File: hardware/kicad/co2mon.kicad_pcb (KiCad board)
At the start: 2 copper layers, 58 x 41 mm, 57 parts, among them J1 SCD30_Conn, J10 TFT_Conn, J11 OLED_Conn, J2 MH_Conn, J3 Z19B_Conn2, J4 T67xx_Conn, J5 Z14A_Conn, J6 Z19B_Conn1, J7 USB_B_Micro, J8 SD_Conn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

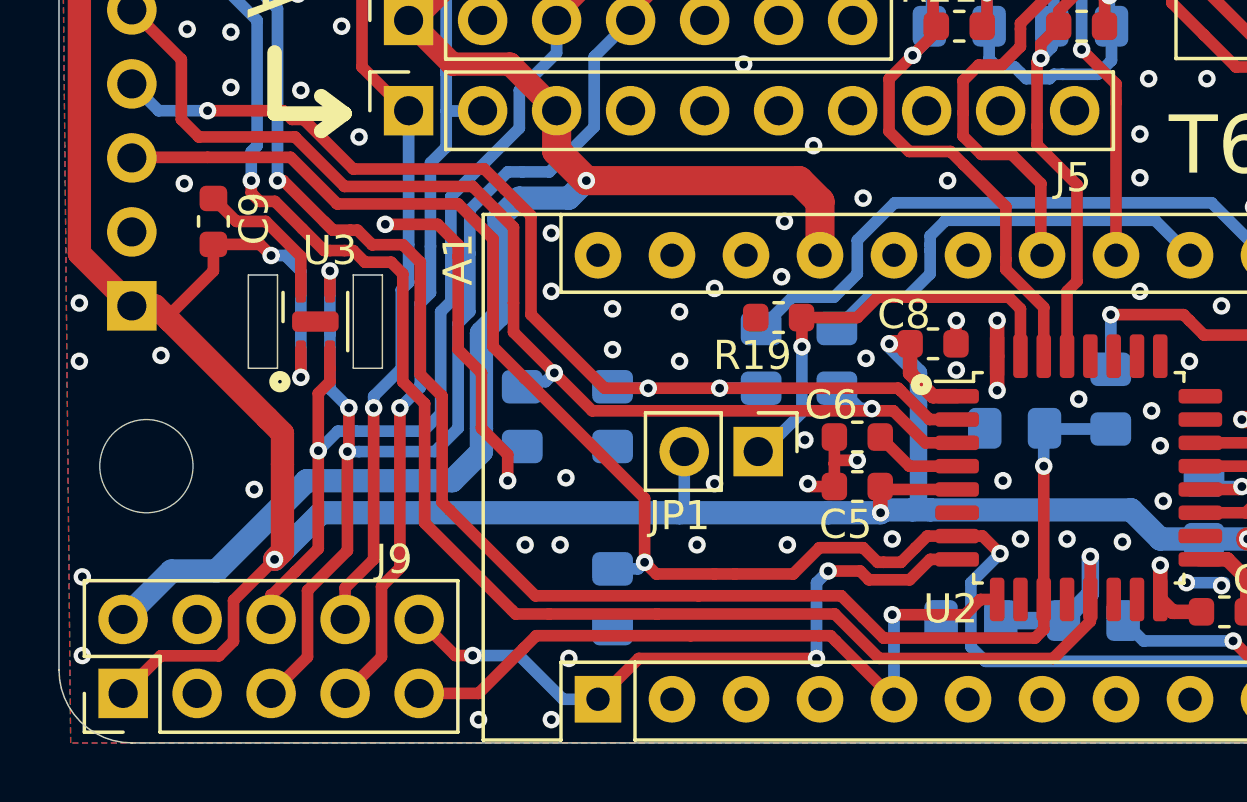
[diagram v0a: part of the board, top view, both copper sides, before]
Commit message: remove temp/humidity sensor
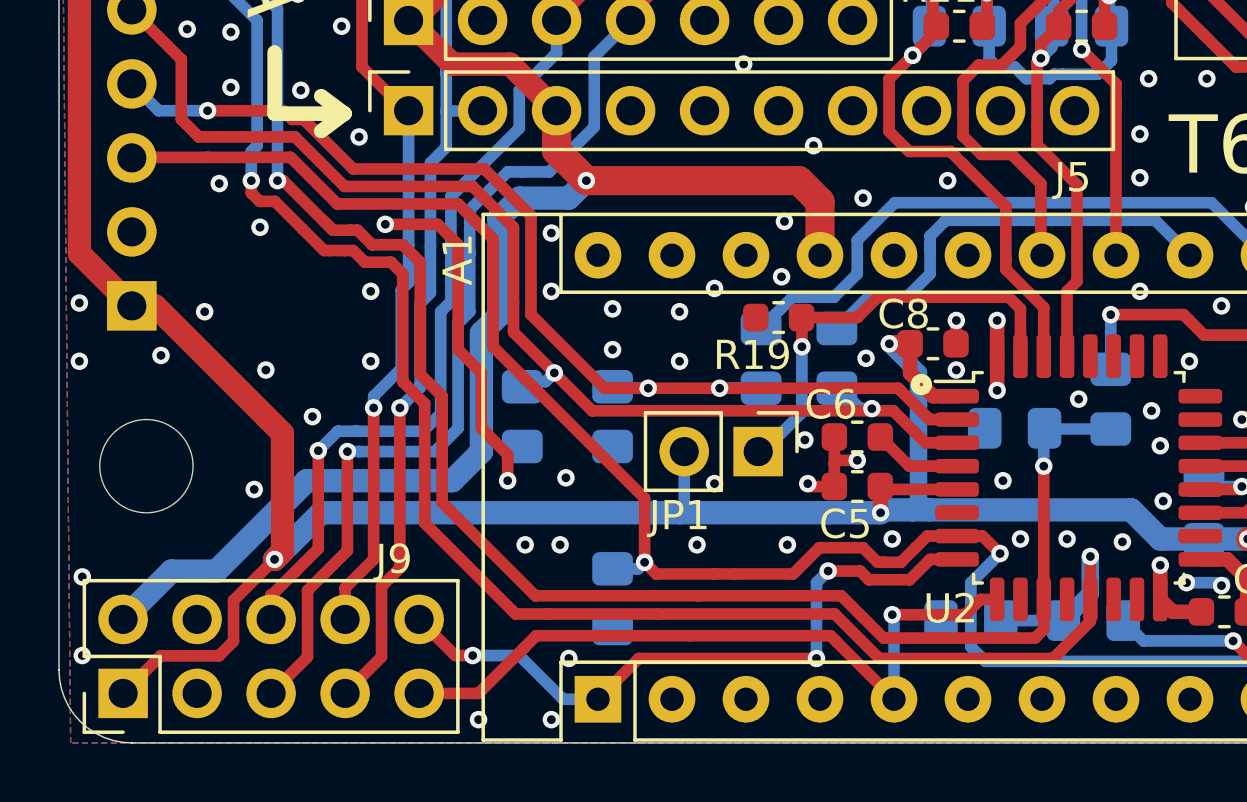
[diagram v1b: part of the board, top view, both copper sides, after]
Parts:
- removed C9: 0.1u, Capacitor_SMD:C_0603_1608Metric
- removed U3: SHTC3, Sensor_Humidity:Sensirion_DFN-4-1EP_2x2mm_P1mm_EP0.7x1.6mm
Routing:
- net +3V3: track 219.0 -> 207.7 mm, vias 12 -> 10
- net /SDA: track 117.7 -> 110.4 mm, vias 4 -> 2
- net GND: track 48.8 -> 43.7 mm, vias 155 -> 161
- net /SCL: track 105.9 -> 102.2 mm
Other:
- outline, holes or cut-outs redrawn
- board text added: "v1b"
- board text removed: "v1"
